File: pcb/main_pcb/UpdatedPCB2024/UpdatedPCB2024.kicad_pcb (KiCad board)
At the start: 2 copper layers, 20 parts, among them J1 Conn_01x05, J2 Conn_01x05, J3 Conn_01x05, J4 Conn_01x05, J5 Conn_01x05, J6 Conn_01x05, J7 Conn_01x05, J8 Conn_01x06_Male, J9 Conn_01x06_Male, U1 Teensy_4.0, U2 DRV8833

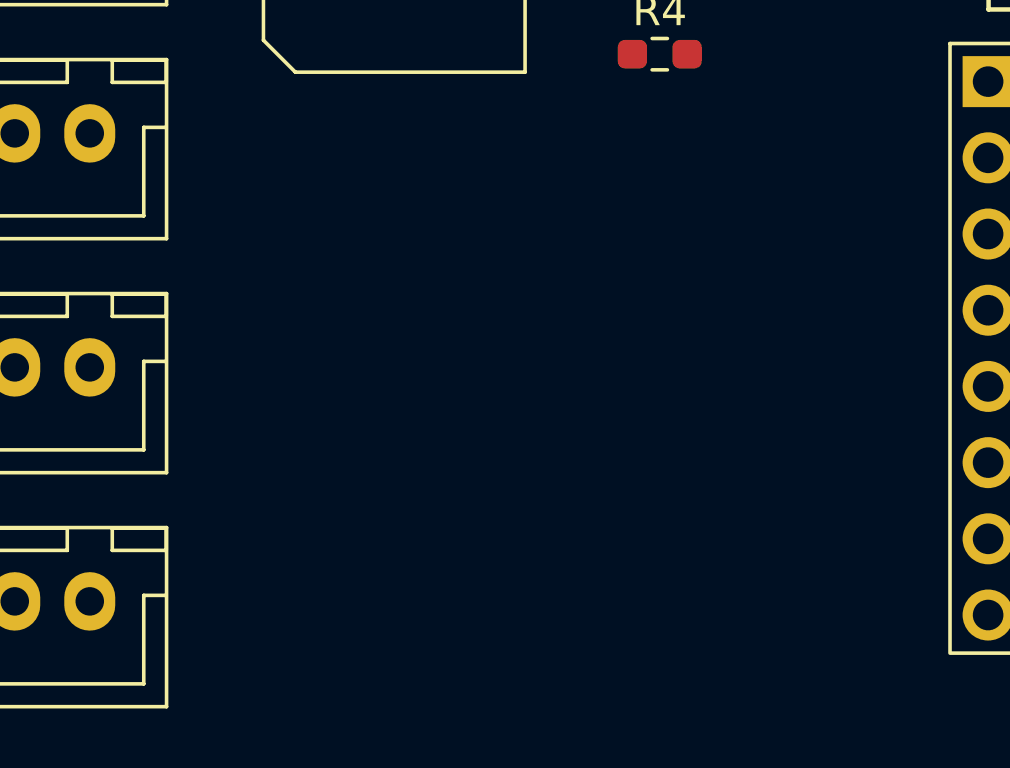
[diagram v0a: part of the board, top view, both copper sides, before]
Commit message: adding footprints continued
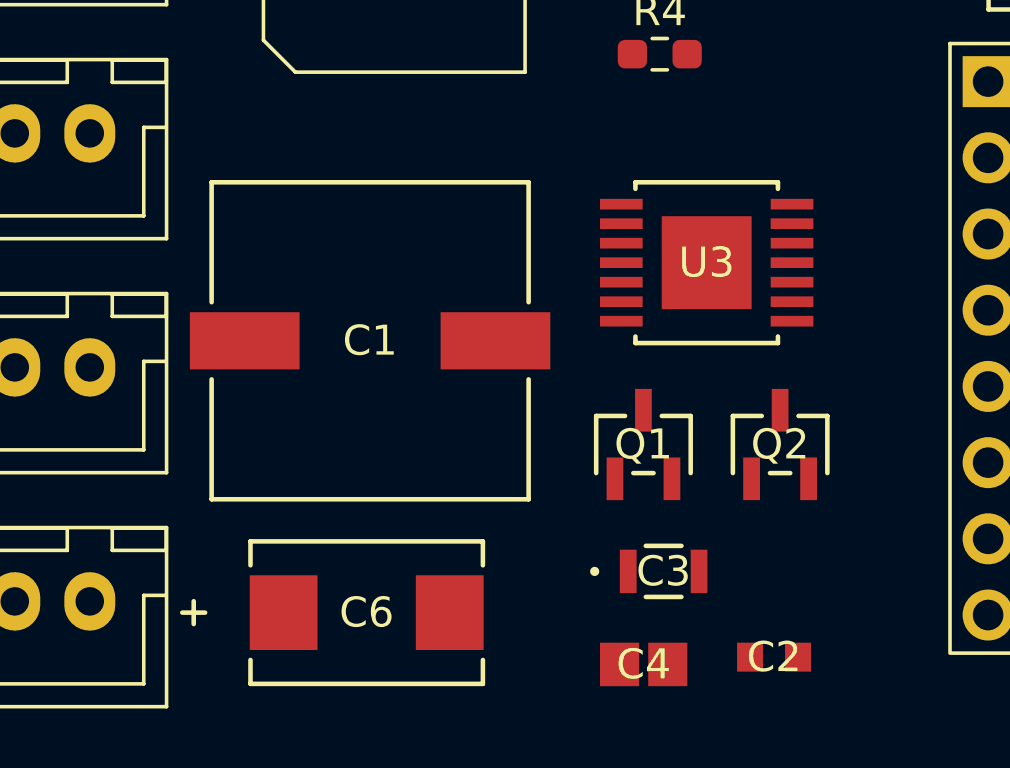
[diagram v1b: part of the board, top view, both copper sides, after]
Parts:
- added C1: 100 µF, custom_footprints:CHEMI-JA0, F.Cu at (163.5, 111.4)
- added C2: 0.068 µF, custom_footprints:0603_AVX, F.Cu at (177.0, 121.9)
- added C3: 0.47 µF, custom_footprints:CAP_2012_TDK, F.Cu at (173.3, 119.1)
- added C4: 1 µF, custom_footprints:CAPC220145_100N_KEM, F.Cu at (172.7, 122.2)
- added C6: 150 µF, custom_footprints:PCAP_EEF_SX_PAN, F.Cu at (163.4, 120.4)
- added Q1: Q_NJFET_DSG, custom_footprints:TRANS_RTR020N_ROM, F.Cu at (172.6, 114.8)
- added Q2: Q_NJFET_DSG, custom_footprints:TRANS_RTR020N_ROM, F.Cu at (177.2, 114.8)
- added U3: LM3151/2/3, custom_footprints:MXA14A_TEX, F.Cu at (174.8, 108.8)

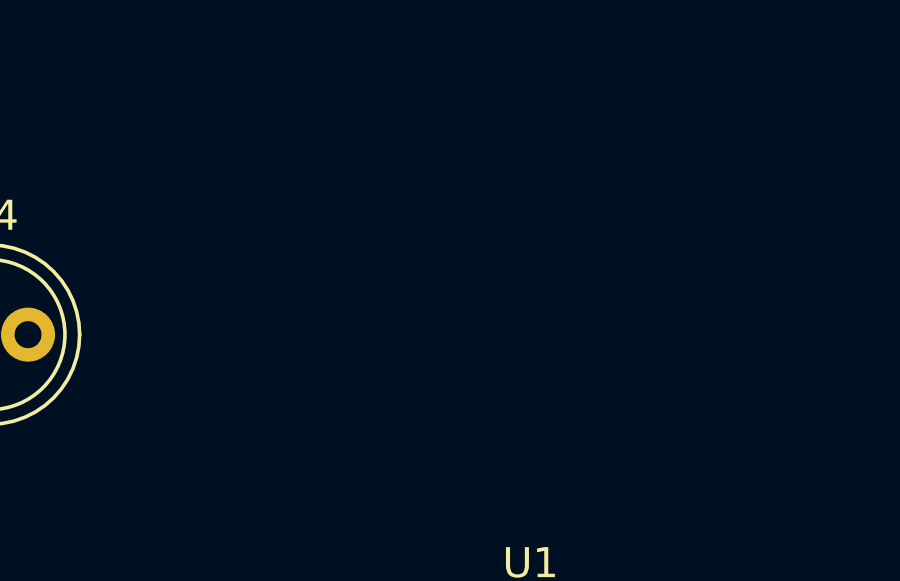
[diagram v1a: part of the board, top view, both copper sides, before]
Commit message: Created L1 footprint
Created L1 footprint from product datasheet's recommended footprint.
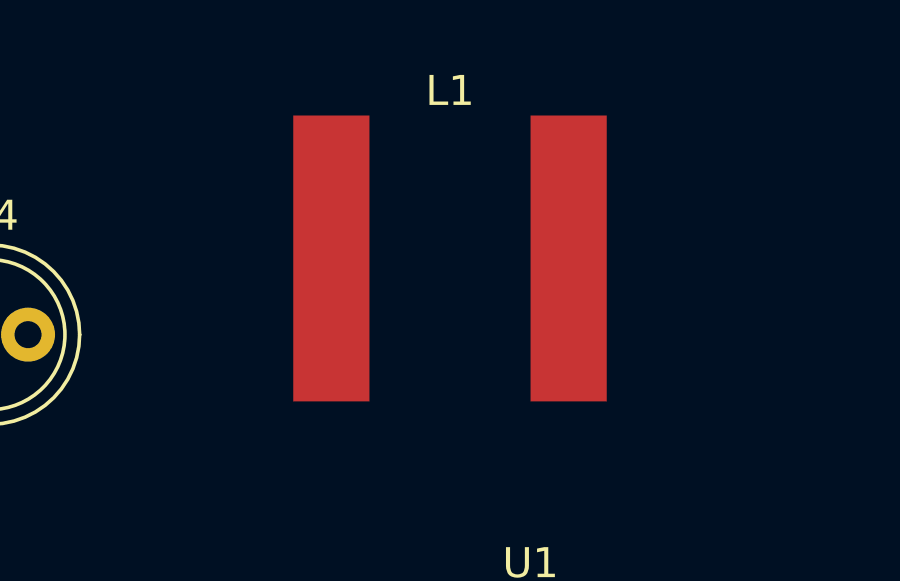
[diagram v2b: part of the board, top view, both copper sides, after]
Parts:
- added L1: 1.65 µH, custom_footprints:HA3778-AL, F.Cu at (199.2, 71.1)
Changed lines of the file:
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@@
     )
+  )
+  (footprint "custom_footprints:HA3778-AL" (layer "F.Cu")
+    (at 199.245 71.12)
+    (property "Sheetfile" "UpdatedPCB2024.kicad_sch")
+    (property "Sheetname" "")
+    (property "ki_description" "Inductor")
+    (property "ki_keywords" "inductor choke coil reactor magnetic")
+    (attr smd)
+    (fp_text reference "L1" (at 0 -5.58 unlocked) (layer "F.SilkS")
+        (effects (font (size 1 1) (thickness 0.1)))
+    )
+    (fp_text value "1.65 µH" (at 0 -7.62 unlocked) (layer "F.Fab")
+        (effects (font (size 1 1) (thickness 0.15)))
+    )
+    (fp_text user "${REFERENCE}" (at 0 5.58 unlocked) (layer "F.Fab")
+        (effects (font (size 1 1) (thickness 0.15)))
+    )
+    (pad "1" smd rect (at -3.955 0) (size 2.54 9.53) (layers "F.Cu" "F.Paste" "F.Mask")
+      (net 50 "Net-(U3-FB)") (pinfunction "1") (pintype "passive") (thermal_bridge_angle 45))
+    (pad "2" smd rect (at 3.955 0) (size 2.54 9.53) (layers "F.Cu" "F.Paste" "F.Mask")
+      (net 48 "Net-(Q1-S)") (pinfunction "2") (pintype "passive") (thermal_bridge_angle 45))
   )
   (footprint "custom_footprints:CHEMI-JA0" (layer "F.Cu")

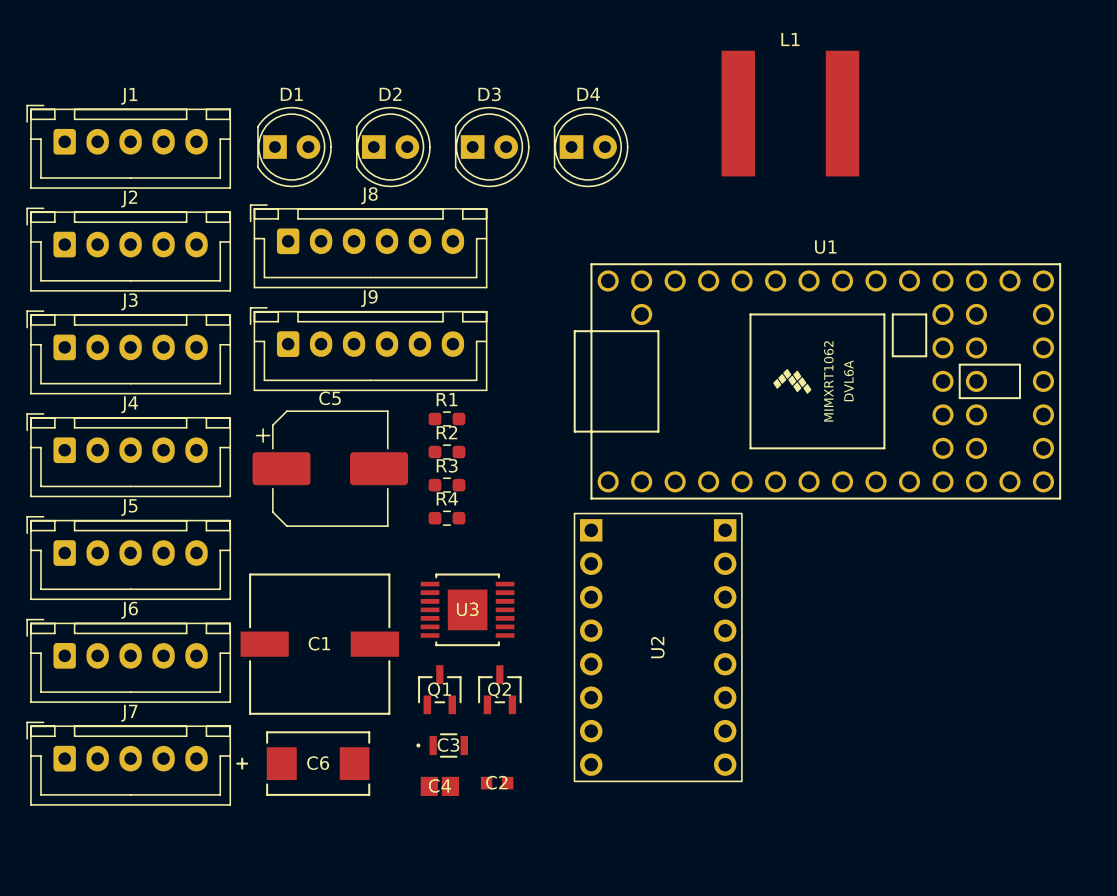
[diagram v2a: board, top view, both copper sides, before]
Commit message: fixing errors on PCB as well as readjustments to outline of PCB
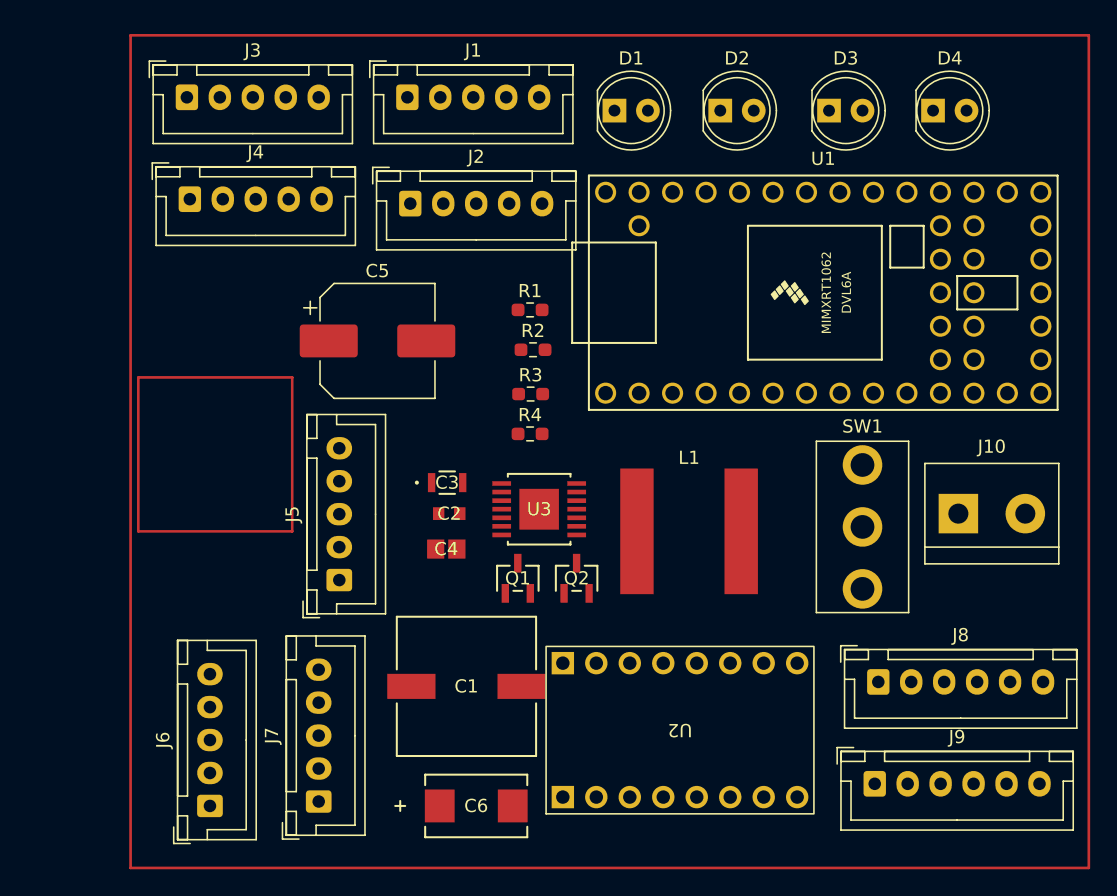
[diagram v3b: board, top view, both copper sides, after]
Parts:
- added J10: Screw_Terminal_01x02, TerminalBlock:TerminalBlock_bornier-2_P5.08mm, F.Cu at (212.0, 101.5)
- added SW1: SW_SPDT, custom_footprints:SW_SPDT_NKK_MS12AANW03, F.Cu at (204.7, 102.5)
- moved J8 55.9 mm to (205.9, 114.2)
- moved J9 55.6 mm to (205.6, 122.0)
- moved L1 32.6 mm to (191.6, 102.8)
- moved D4 27.6 mm to (210.1, 70.9)
- moved D3 27.2 mm to (202.2, 70.9)
- moved D2 26.4 mm to (193.9, 70.9)
- moved J2 26.4 mm to (170.4, 78.0)
- moved J1 26.2 mm to (170.2, 69.9)
- moved D1 25.9 mm to (185.9, 70.9)
- moved J4 21.3 mm to (153.7, 77.6)
- moved J3 21.1 mm to (153.5, 69.9)
- moved J5 20.9 mm to (165.0, 106.5), turned to 90 degrees
- moved C2 20.8 mm to (173.4, 101.5)
- moved C3 19.9 mm to (173.2, 99.1)
- moved J7 19.5 mm to (163.5, 123.3), turned to 90 degrees
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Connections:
- U3 pad 1: Net-(Q2-G) -> Net-(U3-VCC)
- U3 pad 10: Net-(U3-FB) -> Net-(Q1-S)
- U3 pad 11: (no net) -> Net-(Q1-G)
- U3 pad 13: Net-(Q1-S) -> Net-(Q2-G)
- U3 pad 14: (no net) -> GND
- U3 pad 4: Net-(U3-SS) -> Net-(U3-FB)
- U3 pad 5: (no net) -> GND
- U3 pad 6: GND -> Net-(U3-SS)
- U3 pad 8: Net-(U3-VCC) -> (no net)
- U3 pad 9: Net-(Q1-G) -> (no net)

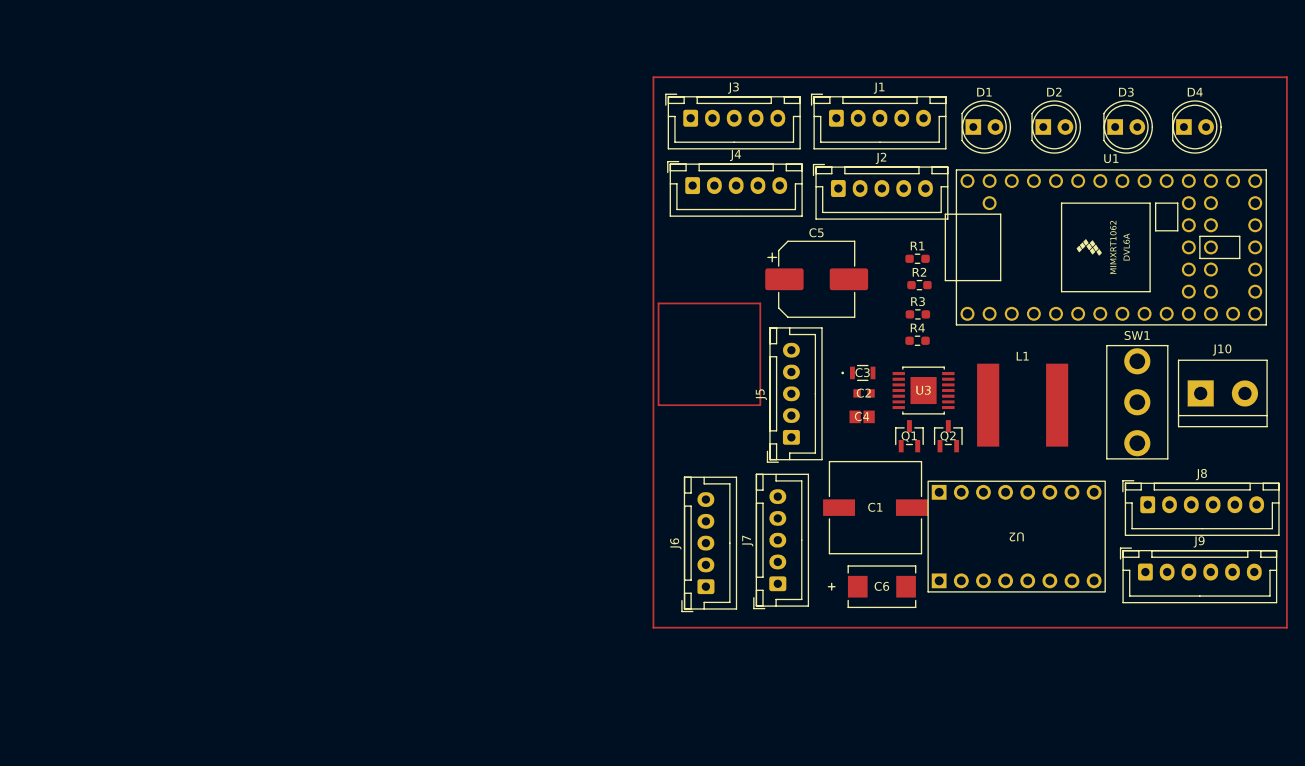
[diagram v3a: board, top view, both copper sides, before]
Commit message: Simple switch controller layout
Did the layout for the simple switch controller such that the pathing is easy.
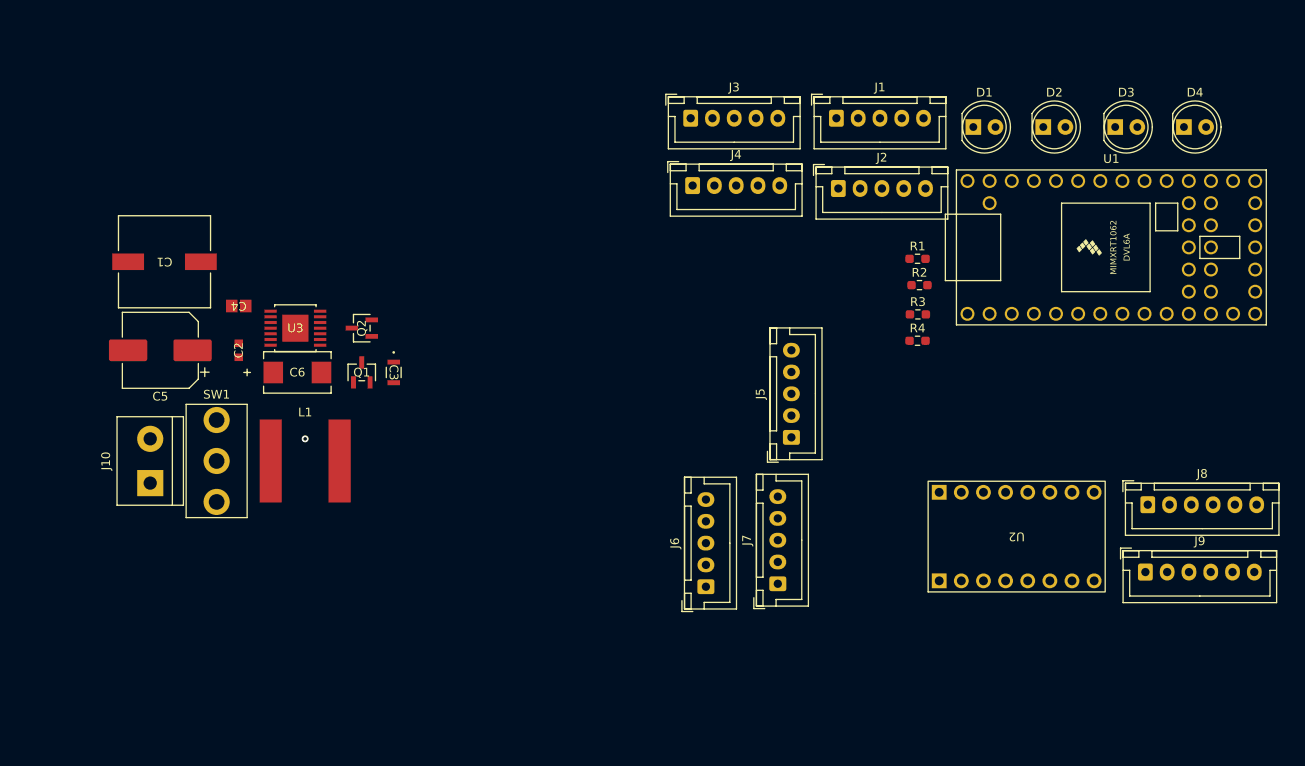
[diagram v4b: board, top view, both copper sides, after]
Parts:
- moved J10 121.0 mm to (91.4, 111.8), turned to 90 degrees
- moved SW1 105.9 mm to (99.1, 109.2)
- moved C1 86.3 mm to (93.1, 86.4), turned to 180 degrees
- moved L1 82.6 mm to (109.2, 109.2)
- moved C5 75.8 mm to (92.6, 96.5), turned to 180 degrees
- moved C4 72.7 mm to (101.6, 91.4), turned to 180 degrees
- moved U3 72.4 mm to (108.1, 94.0)
- moved C2 71.9 mm to (101.6, 96.5), turned to 90 degrees
- moved C6 71.4 mm to (108.3, 99.1)
- moved Q2 68.4 mm to (115.7, 94.0), turned to 90 degrees
- moved Q1 63.3 mm to (115.7, 99.1)
- moved C3 53.8 mm to (119.4, 99.1), turned to -90 degrees
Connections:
- C4 pad 1: Net-(U3-VCC) -> /5V
- U1 pad Vin: +BATT -> /5V
- U3 pad 1: Net-(U3-VCC) -> /5V
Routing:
- net GND: vias 0 -> 1

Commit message: Edited schematic + layout
Changed some pin configurations (made sure SDA and SCL are configured properly, as well as all PWM necessary pins) and began routing. Layout at this point is finalized, needs to be reviewed and approved. All LIDARs located on one side of board, and both motor attachments located on the other. Board size is still TBD.
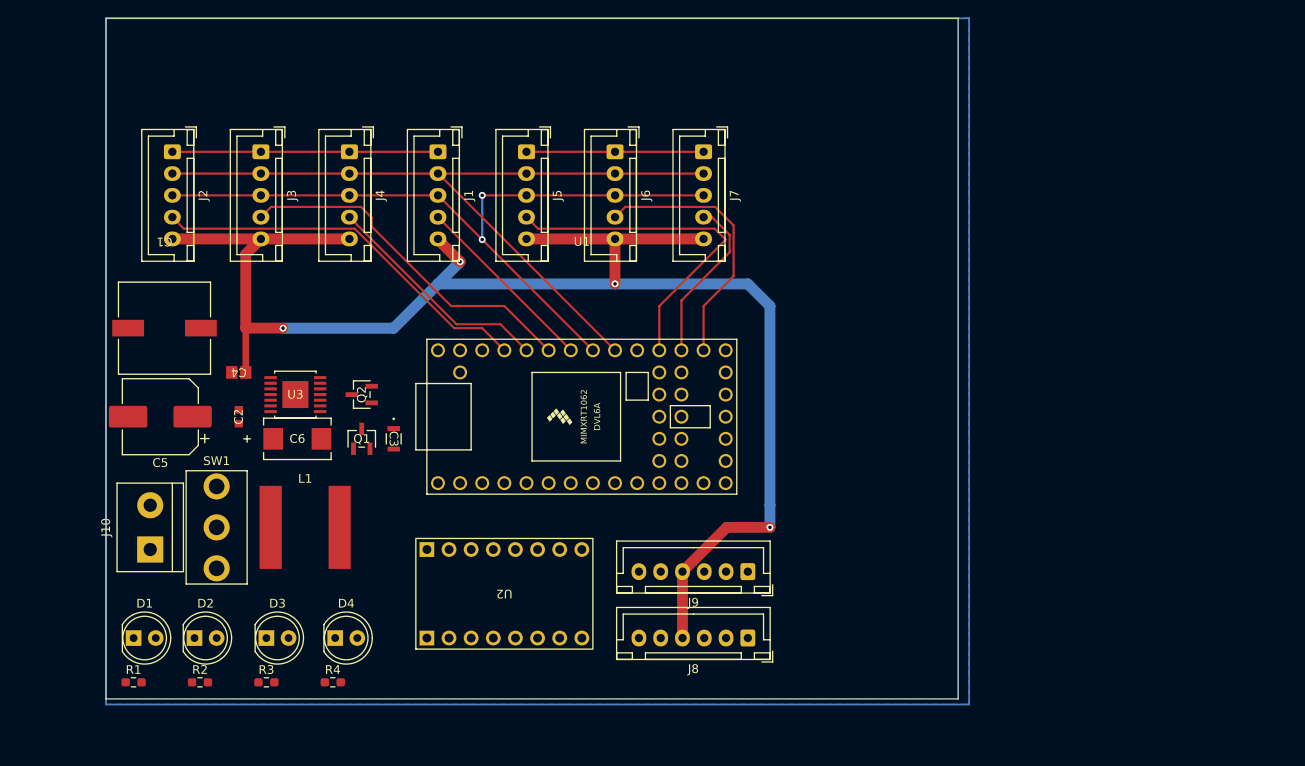
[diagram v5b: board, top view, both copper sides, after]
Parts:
- moved D2 113.7 mm to (96.5, 129.5)
- moved D3 113.7 mm to (104.8, 129.5)
- moved D4 113.7 mm to (112.7, 129.5)
- moved D1 112.8 mm to (89.5, 129.5)
- moved R1 102.3 mm to (89.5, 134.6)
- moved R2 94.3 mm to (97.2, 134.6)
- moved R3 85.9 mm to (104.8, 134.6)
- moved R4 77.7 mm to (112.4, 134.6)
- moved J2 76.5 mm to (94.0, 73.7), turned to -90 degrees
- moved U1 63.8 mm to (141.0, 104.1)
- moved U2 59.2 mm to (132.1, 124.5)
- moved J6 51.0 mm to (144.8, 73.7), turned to -90 degrees
- moved J7 50.3 mm to (154.9, 73.7), turned to -90 degrees
- moved J3 49.5 mm to (104.1, 73.7), turned to -90 degrees
- moved J8 48.4 mm to (160.0, 129.5), turned to 180 degrees
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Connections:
- C4 pad 1: /5V -> +3V3
- J1 pad 2: /SDA2 -> /SDA0
- J1 pad 3: /SCL2 -> /SCL0
- J2 pad 2: /SDA2 -> /SDA0
- J2 pad 3: /SCL2 -> /SCL0
- J3 pad 2: /SDA2 -> /SDA0
- J3 pad 3: /SCL2 -> /SCL0
- J4 pad 2: /SDA2 -> /SDA0
- J4 pad 3: /SCL2 -> /SCL0
- J5 pad 2: /SDA2 -> /SDA0
- J5 pad 3: /SCL2 -> /SCL0
- J6 pad 2: /SDA2 -> /SDA0
- J6 pad 3: /SCL2 -> /SCL0
- J7 pad 2: /SDA2 -> /SDA0
- J7 pad 3: /SCL2 -> /SCL0
- U1 pad 0: /BEQ1 -> unconnected-(U1-IO0-Pad0)
- U1 pad 1: /BEQ2 -> /LED0
- U1 pad 10: unconnected-(U1-IO10-Pad10) -> /AEQ1
- U1 pad 11: /AEQ1 -> /BEQ2
- U1 pad 14: /LCS7 -> /LCS6
- U1 pad 15: /LCS6 -> /LCS7
- U1 pad 17: /SCL2 -> unconnected-(U1-IO17-Pad17)
- U1 pad 18: /LCS1 -> /SDA0
- U1 pad 19: /LED3 -> /SCL0
- U1 pad 2: /AIN1 -> /LED1
- U1 pad 20: /LED2 -> /LCS1
- U1 pad 21: unconnected-(U1-IO21-Pad21) -> /LCS3
- U1 pad 22: /LCS3 -> /LCS4
- U1 pad 3: /BIN2 -> /LED2
- U1 pad 4: /LED0 -> /LED3
- U1 pad 5: /LED1 -> /BIN1
- U1 pad 6: /LCS4 -> /BIN2
- U1 pad 7: unconnected-(U1-IO7-Pad7) -> /AIN2
- U1 pad 8: /BIN1 -> /AIN1
- U1 pad 9: /AIN2 -> /BEQ1
- U1 pad Vin: /5V -> +BATT
- U3 pad 1: /5V -> +3V3
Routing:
- net +3V3: track 0.00 -> 177.6 mm, vias 0 -> 4
- net /SDA0: track 0.00 -> 89.7 mm
- net /SCL0: track 0.00 -> 86.1 mm, vias 0 -> 2
- net GND: track 0.00 -> 50.8 mm, vias 1 -> 0
- net /LCS2: track 0.00 -> 44.4 mm
- net /LCS3: track 0.00 -> 40.9 mm
- net /LCS5: track 0.00 -> 39.8 mm
- net /LCS6: track 0.00 -> 30.7 mm
- net /LCS4: track 0.00 -> 26.6 mm
- net /LCS1: track 0.00 -> 21.6 mm
- net /LCS7: track 0.00 -> 19.4 mm
- added copper zone on B.Cu, net GND
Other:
- board outline added: 97.8 x 78.1 mm
